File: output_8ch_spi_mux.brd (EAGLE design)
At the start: 65 x 56 mm, 44 parts, among them IC1 TPS706-1V8, IC2 5M160ZE64, IC3 SN75174SOIC-20, IC4 SN75174SOIC-20, IC6 MCP2517FDSOIC-14, IC7 CAT24C256, Q1 50MHz, Q2 20MHz

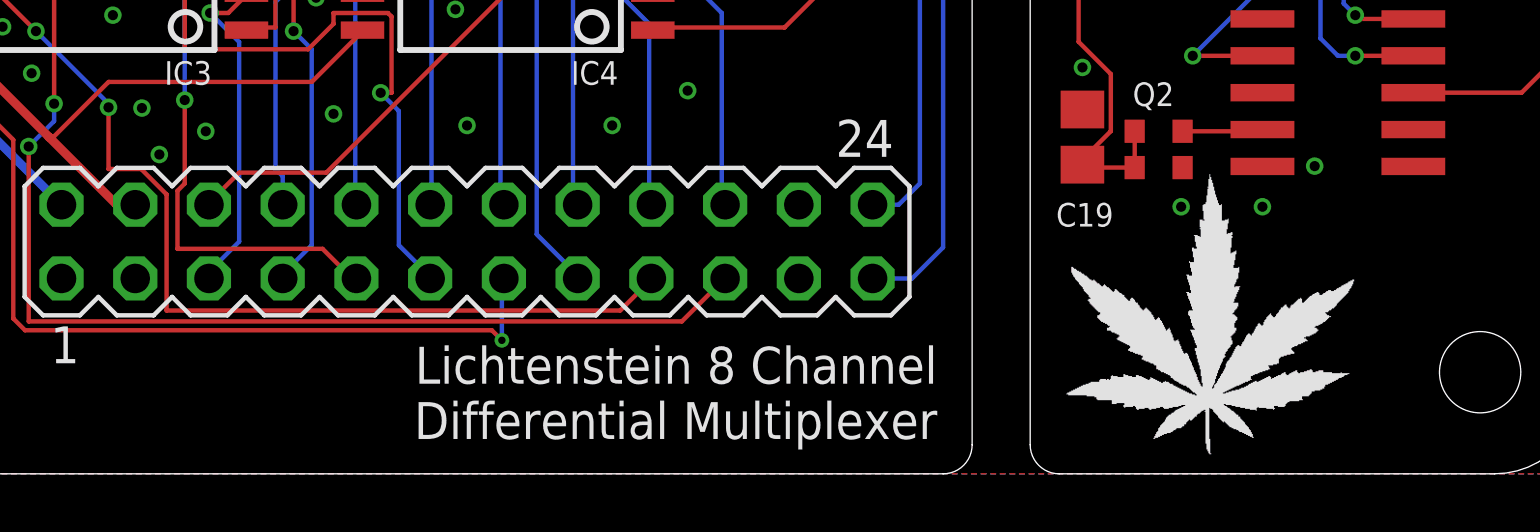
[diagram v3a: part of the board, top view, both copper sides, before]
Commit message: routed differential output board
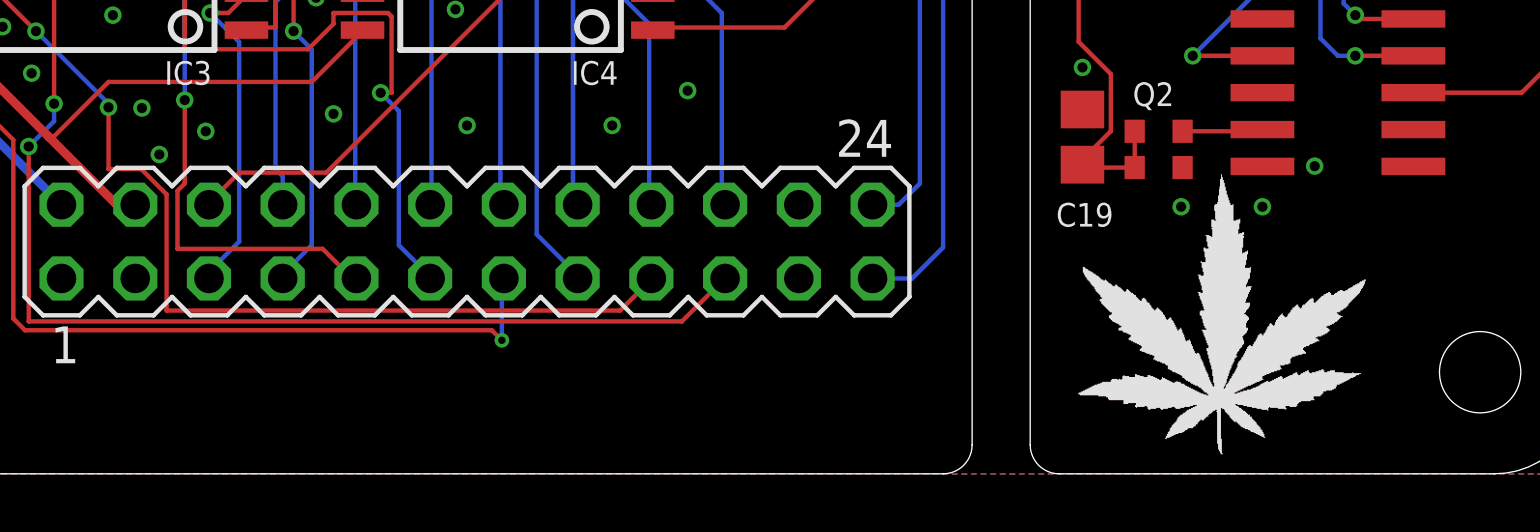
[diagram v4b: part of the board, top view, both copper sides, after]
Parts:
- moved WEED1 0.40 mm to (47.6, 0.59)
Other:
- board text added: "(c) 2018 Tristan Seifert"
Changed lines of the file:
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@@
 <wire x1="44" y1="1" x2="43" y2="0" width="0" layer="20" curve="-90"/>
 <wire x1="46" y1="1" x2="47" y2="0" width="0" layer="20" curve="90"/>
-<text x="42.8" y="1.2" size="1.27" layer="25" font="vector" ratio="10" align="bottom-right">Lichtenstein 8 Channel
+<text x="43.2" y="1.2" size="1.27" layer="51" font="vector" ratio="10" align="bottom-right">Lichtenstein 8 Channel
 Differential Multiplexer</text>
 <text x="22.8" y="35.2" size="0.8128" layer="51" font="vector" ratio="10" align="top-center">VCORE Good</text>
+<text x="6.6" y="1.2" size="1.016" layer="51">(c) 2018 Tristan Seifert</text>
 </plain>
 <attributes>
@@
 <attribute name="VALUE" x="15.191" y="39.2" size="1.27" layer="27" ratio="10" rot="R90"/>
 </element>
-<element name="WEED1" library="lichtenstein_onion" package="DOINK" value="WEED" x="47.23" y="0.59" smashed="yes"/>
+<element name="WEED1" library="lichtenstein_onion" package="DOINK" value="WEED" x="47.63" y="0.59" smashed="yes"/>
 <element name="SV3" library="FLYFISH" package="PIN_20X2" value="PIN20X2" x="32.5" y="52.5" smashed="yes">
 <attribute name="MOUSER" value="517-929975-01-20" x="32.5" y="52.5" size="1.778" layer="27" display="off"/>

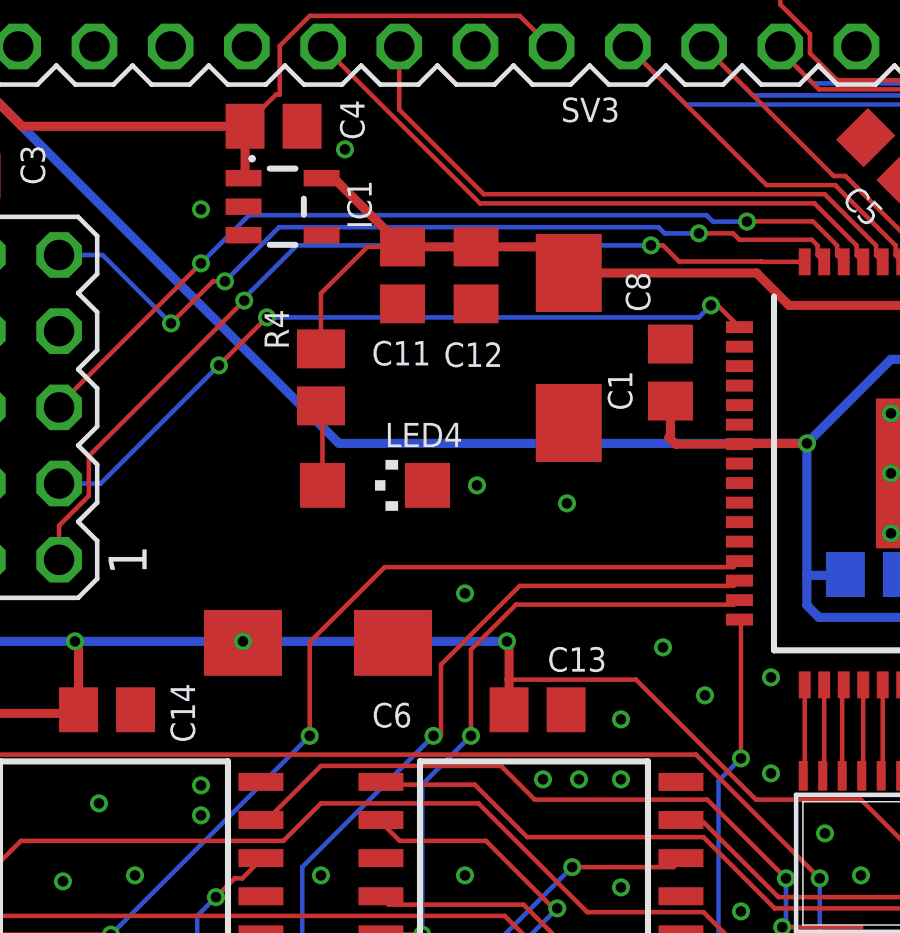
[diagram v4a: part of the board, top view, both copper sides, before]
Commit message: added holes to differential output board
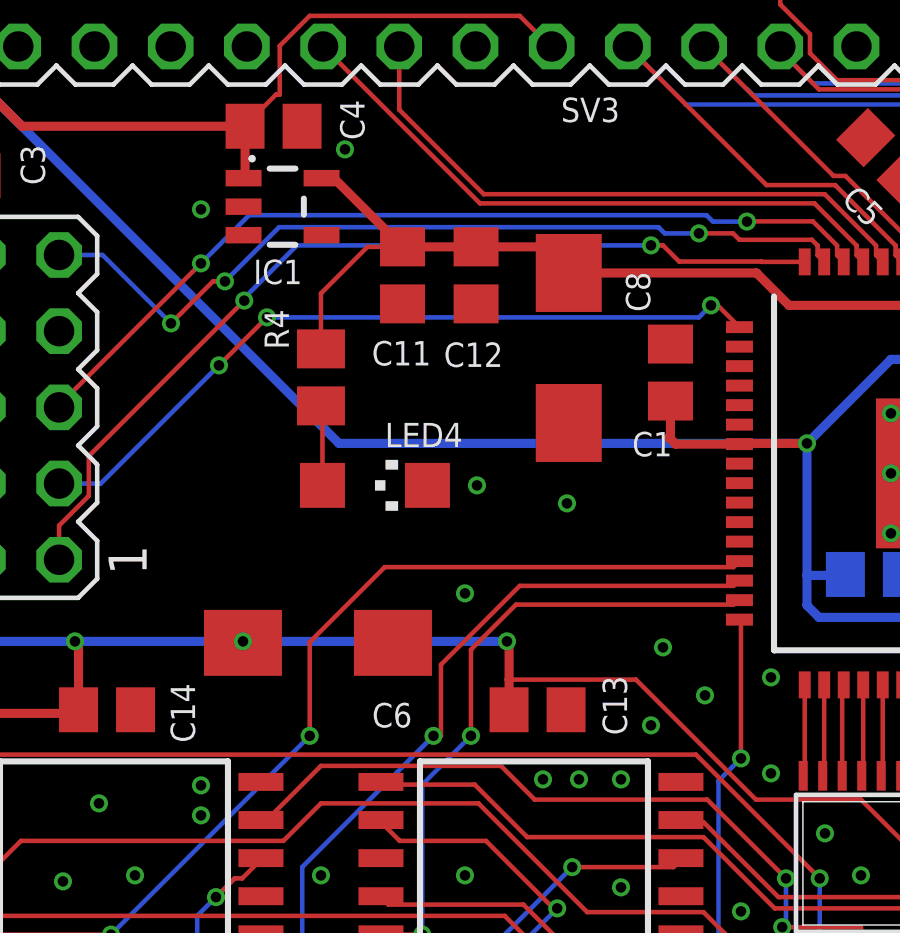
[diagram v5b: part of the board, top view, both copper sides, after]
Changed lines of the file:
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@@
 <?xml version="1.0" encoding="utf-8"?>
 <!DOCTYPE eagle SYSTEM "eagle.dtd">
-<eagle version="9.1.3">
+<eagle version="9.2.1">
 <drawing>
 <settings>
@@
 <element name="C1" library="rcl" library_urn="urn:adsk.eagle:library:334" package="C0805" package3d_urn="urn:adsk.eagle:package:23617/2" value="100nF" x="32.65" y="40.36" smashed="yes" rot="R90">
 <attribute name="MOUSER" value="710-885012207072" x="32.65" y="40.36" size="1.778" layer="27" rot="R90" display="off"/>
-<attribute name="NAME" x="31.38" y="39.09" size="0.8128" layer="25" font="vector" ratio="10" rot="R90"/>
+<attribute name="NAME" x="32.71" y="38.38" size="0.8128" layer="25" font="vector" ratio="10" rot="R180"/>
 <attribute name="SPICEPREFIX" value="C" x="32.65" y="40.36" size="1.778" layer="27" rot="R90" display="off"/>
 </element>
@@
 <element name="C13" library="rcl" library_urn="urn:adsk.eagle:library:334" package="C0805" package3d_urn="urn:adsk.eagle:package:23617/2" value="100nF" x="28.22" y="29.12" smashed="yes">
 <attribute name="MOUSER" value="710-885012207072" x="28.22" y="29.12" size="1.778" layer="27" display="off"/>
-<attribute name="NAME" x="28.55" y="30.39" size="0.8128" layer="25" font="vector" ratio="10"/>
+<attribute name="NAME" x="30.39" y="30.25" size="0.8128" layer="25" font="vector" ratio="10" rot="R270"/>
 <attribute name="SPICEPREFIX" value="C" x="28.22" y="29.12" size="1.778" layer="27" display="off"/>
 </element>
@@
 <element name="IC1" library="lichtenstein_onion" package="SOT23-5" value="TPS706-1V8" x="19.72" y="45.89" smashed="yes" rot="R270">
 <attribute name="MOUSER" value="595-TPS70618DBVT" x="19.72" y="45.89" size="1.778" layer="27" rot="R270" display="off"/>
-<attribute name="NAME" x="21.879" y="46.779" size="0.8128" layer="25" font="vector" ratio="10" rot="R270"/>
+<attribute name="NAME" x="20.379" y="44.121" size="0.8128" layer="25" font="vector" ratio="10" rot="R180"/>
 </element>
 <element name="IC4" library="lichtenstein_onion" package="SOIC20S" value="SN75174SOIC-20" x="28" y="21" smashed="yes" rot="R90">
@@
 <via x="31.6" y="12" extent="1-16" drill="0.35"/>
 <via x="26.6" y="12" extent="1-16" drill="0.35"/>
-<via x="31" y="28.8" extent="1-16" drill="0.35"/>
+<via x="32" y="28.6" extent="1-16" drill="0.35"/>
 <via x="35" y="22.4" extent="1-16" drill="0.35"/>
 <via x="31" y="23.2" extent="1-16" drill="0.35"/>

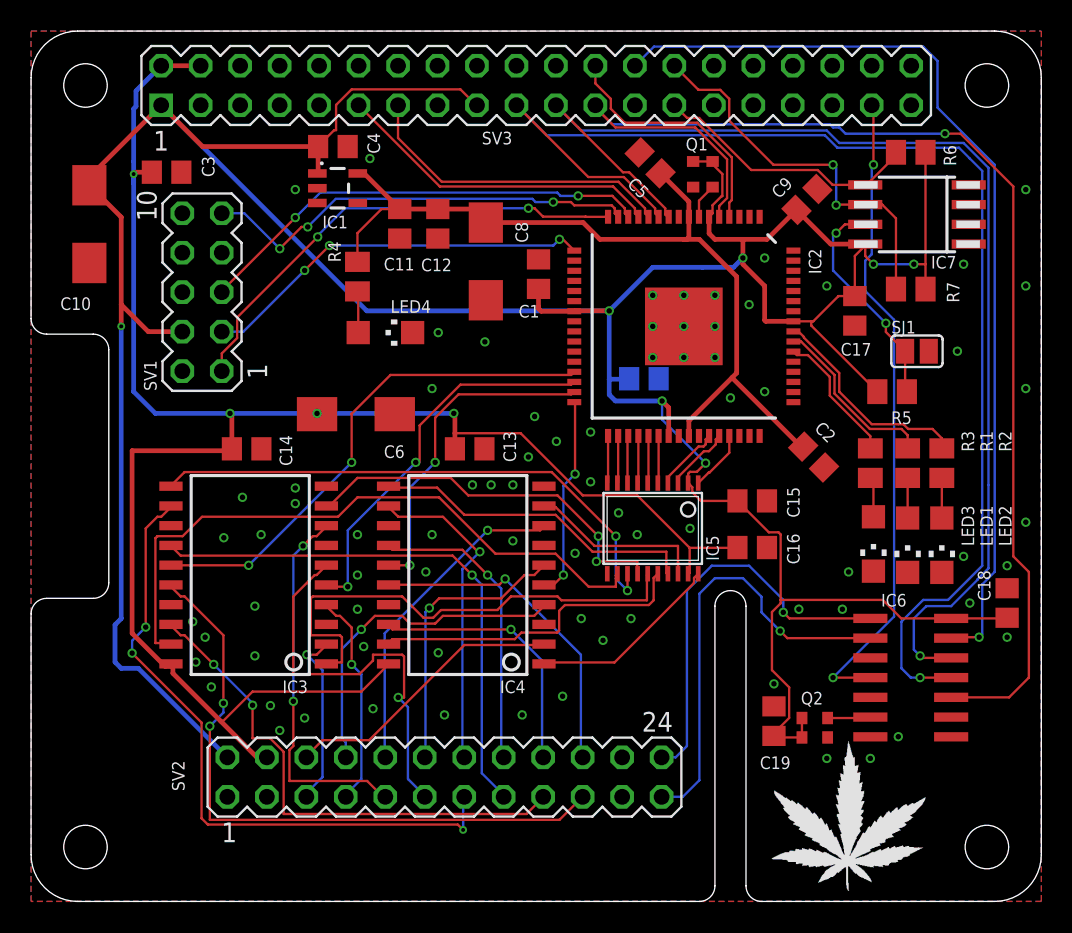
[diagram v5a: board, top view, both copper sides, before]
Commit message: Added STM32 as CAN bus controller to rpi board
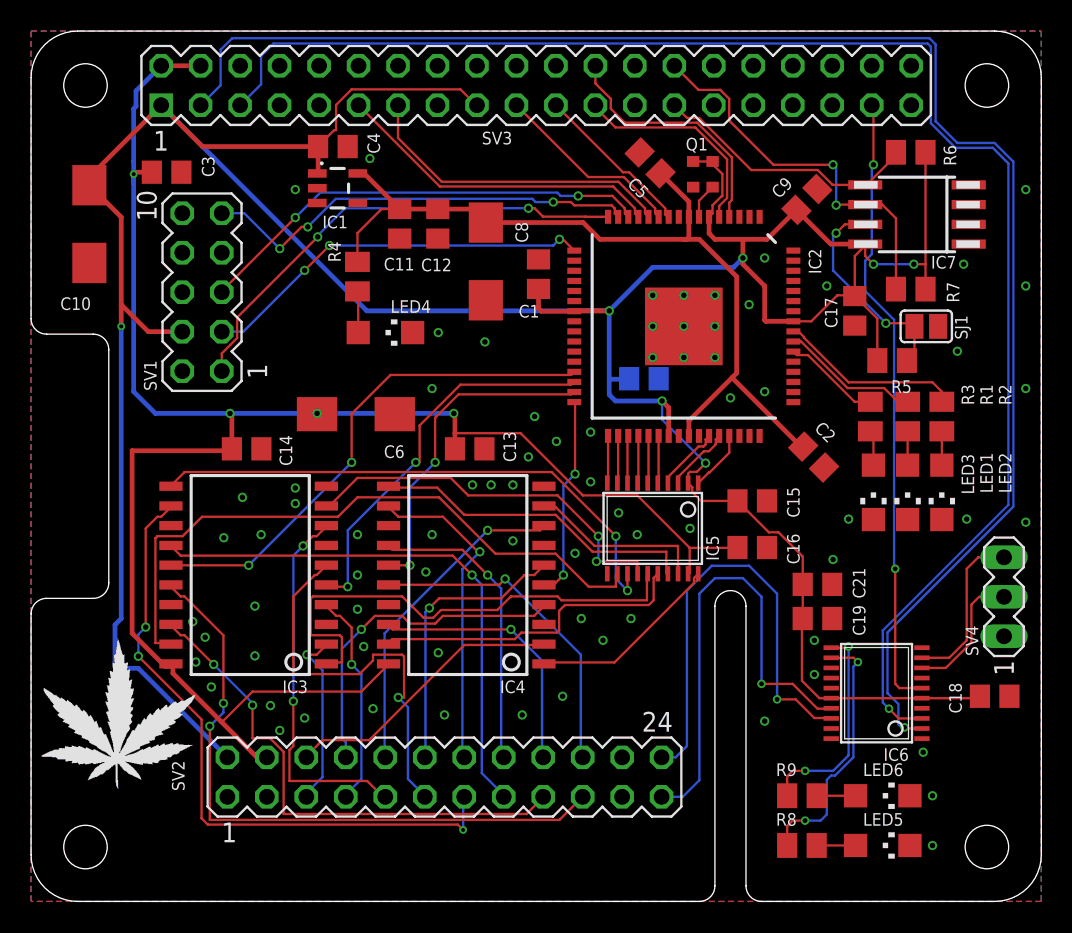
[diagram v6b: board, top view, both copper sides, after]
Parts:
- removed Q2: 20MHz, lichtenstein_onion:VLGA-4
- added C21: 4.7µF, rcl:C0805
- added LED5, LED6: (no value), led:CHIPLED_1206
- added R8, R9: 680R, rcl:M0805
- added SV4: (no value), con-lstb:MA03-1
- IC6: value MCP2517FDSOIC-14 -> STM32F042F; device lichtenstein_onion:SO-14 -> lichtenstein_onion:TSSOP20
- moved WEED1 47.5 mm to (0.63, 7.19)
- moved C19 7.17 mm to (50.6, 18.2), turned to 0 degrees
- moved C18 6.05 mm to (62.0, 13.2), turned to 0 degrees
- moved LED1 3.40 mm to (56.4, 26.3)
- moved LED2 3.40 mm to (58.6, 26.3)
- moved LED3 3.32 mm to (54.2, 26.3)
- moved R1 3.00 mm to (56.4, 31.2)
- moved R2 3.00 mm to (58.6, 31.2)
- moved R3 3.00 mm to (54.0, 31.2)
- moved IC6 2.42 mm to (54.4, 13.4), turned to 90 degrees
- moved R5 2.00 mm to (55.4, 34.8)
- moved SJ1 1.71 mm to (57.6, 37.0)
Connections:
- removed net CLK_20: IC6.6, Q2.3
- new net !CORTEX_RST: IC6.4
- new net CORTEX_STATUS0: IC6.12, R8.1
- new net CORTEX_STATUS1: IC6.11, R9.1
- new net CORTEX_SWCLK: IC6.20
- new net CORTEX_SWDIO: IC6.19
- new net CORTEX_UART_RX: IC6.9, SV4.3
- new net CORTEX_UART_TX: IC6.8, SV4.2
- new net N$4: LED5.A, R8.2
- new net N$5: LED6.A, R9.2
- net !CAN_INT: now also IC6.6; no longer IC6.4
- net !SPI_CS1: no longer IC6.13
- net +3V3: now also C21.1, IC6.16, IC6.5; no longer IC6.14, Q2.1, Q2.4
- net CAN_RX: now also IC6.17; no longer IC6.2
- net CAN_TX: now also IC6.18; no longer IC6.1
- net GND: now also C21.2, IC6.1, IC6.15, LED5.C, LED6.C, SV4.1; no longer IC6.7, Q2.2
- net I2C_SCL: now also IC6.3
- net I2C_SDA: now also IC6.2
- net SPI_MISO: no longer IC6.12
- net SPI_MOSI: no longer IC6.11
- net SPI_SCK: no longer IC6.10
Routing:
- net I2C_SDA: track 0.00 -> 103.1 mm, vias 0 -> 1
- net I2C_SCL: track 0.00 -> 99.2 mm, vias 0 -> 1
- net SPI_MOSI: track 82.6 -> 12.3 mm, vias 1 -> 0
- net SPI_SCK: track 80.6 -> 14.0 mm, vias 1 -> 0
- net SPI_MISO: track 76.5 -> 10.5 mm, vias 1 -> 0
- net !SPI_CS1: track 61.2 -> 0.00 mm, vias 1 -> 0
- net CORTEX_STATUS0: track 0.00 -> 16.7 mm, vias 0 -> 2
- net CORTEX_STATUS1: track 0.00 -> 13.9 mm, vias 0 -> 2
- net +3V3: track 243.5 -> 231.5 mm
- net CORTEX_UART_RX: track 0.00 -> 10.7 mm
- net CORTEX_UART_TX: track 0.00 -> 8.60 mm
- net CAN_TX: track 26.3 -> 29.9 mm
- net CLK_20: track 2.77 -> 0.00 mm
- net N$5: track 0.00 -> 2.50 mm
- net N$4: track 0.00 -> 2.50 mm
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
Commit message: Added cortex debug header
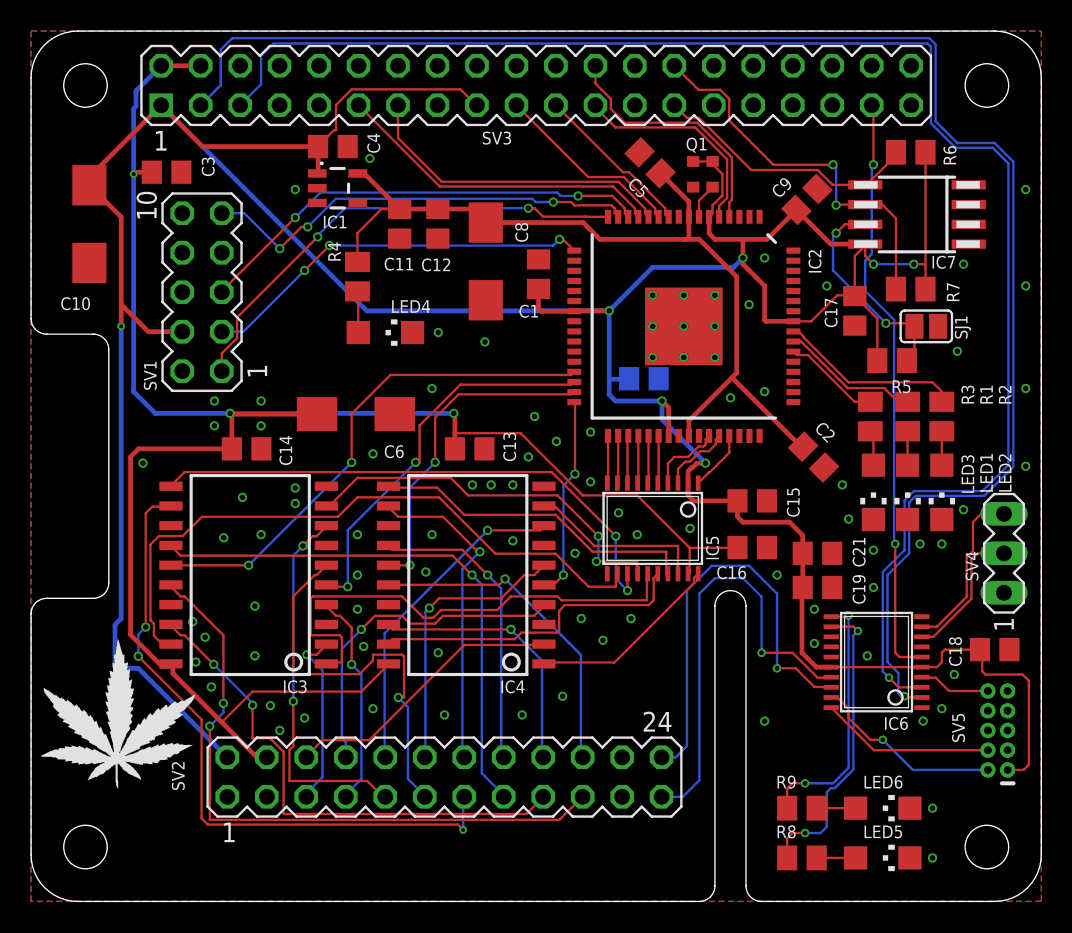
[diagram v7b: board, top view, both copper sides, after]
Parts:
- added SV5: CORTEX_DEBUG_PTH, lichtenstein_onion:2X5-PTH-1.27MM
- moved C18 3.00 mm to (62.0, 16.2)
- moved SV4 2.80 mm to (62.6, 22.4)
- moved C19 2.00 mm to (50.6, 20.2)
- moved C21 2.00 mm to (50.6, 22.4)
- moved IC6 2.00 mm to (54.4, 15.4)
- moved LED5 0.80 mm to (54.8, 2.80)
- moved R8 0.80 mm to (49.6, 2.80)
- moved LED6 0.80 mm to (54.8, 6.00)
- moved R9 0.80 mm to (49.6, 6.00)
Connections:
- net !CORTEX_RST: now also SV5.10
- net +3V3: now also SV5.1
- net CORTEX_SWCLK: now also SV5.4
- net CORTEX_SWDIO: now also SV5.2
- net GND: now also SV5.3, SV5.5, SV5.9
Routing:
- net CORTEX_SWDIO: track 0.00 -> 12.4 mm, vias 0 -> 1
- net +3V3: track 231.5 -> 243.8 mm
- net CORTEX_SWCLK: track 0.00 -> 11.2 mm
- net +5V: track 118.0 -> 122.9 mm, vias 4 -> 3
- net !CORTEX_RST: track 0.00 -> 4.61 mm
- net CORTEX_STATUS0: track 16.7 -> 19.5 mm
- net CORTEX_STATUS1: track 13.9 -> 16.7 mm
- net CAN_TX: track 29.9 -> 27.9 mm
- net CAN_RX: track 30.5 -> 28.5 mm
- net !CAN_INT: track 40.1 -> 38.1 mm
- net I2C_SCL: track 99.2 -> 99.8 mm
- net I2C_SDA: track 103.1 -> 103.6 mm
- net OUT6_P: track 42.1 -> 42.6 mm
- net OUT_3V2: track 4.32 -> 4.83 mm
